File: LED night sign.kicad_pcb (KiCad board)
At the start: 2 copper layers, 42.9 x 36.7 mm, 38 parts, among them Q1 MOSFET-NCH-2N7002PW, Q2 BC817, U1 ATtiny85-20M, U2 APDS-9301

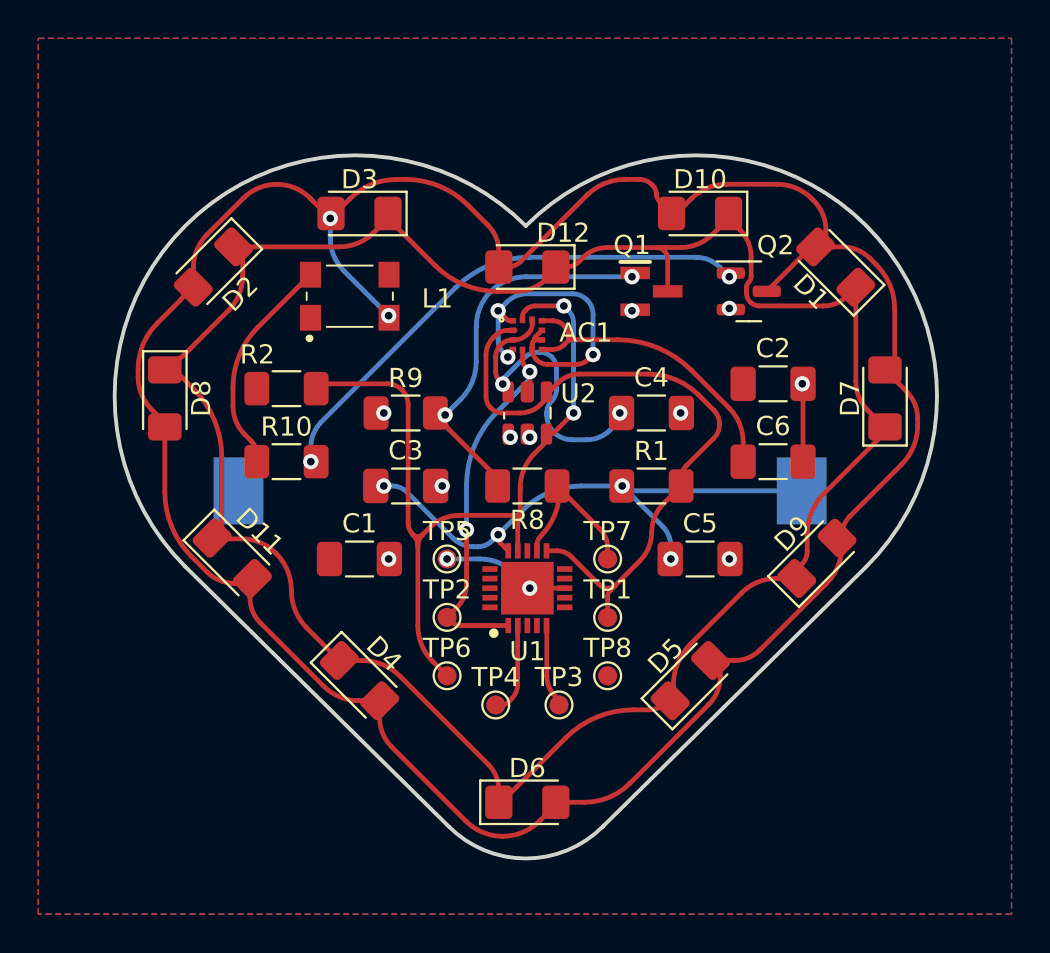
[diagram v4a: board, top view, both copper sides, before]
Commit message: Improved pcb wiring
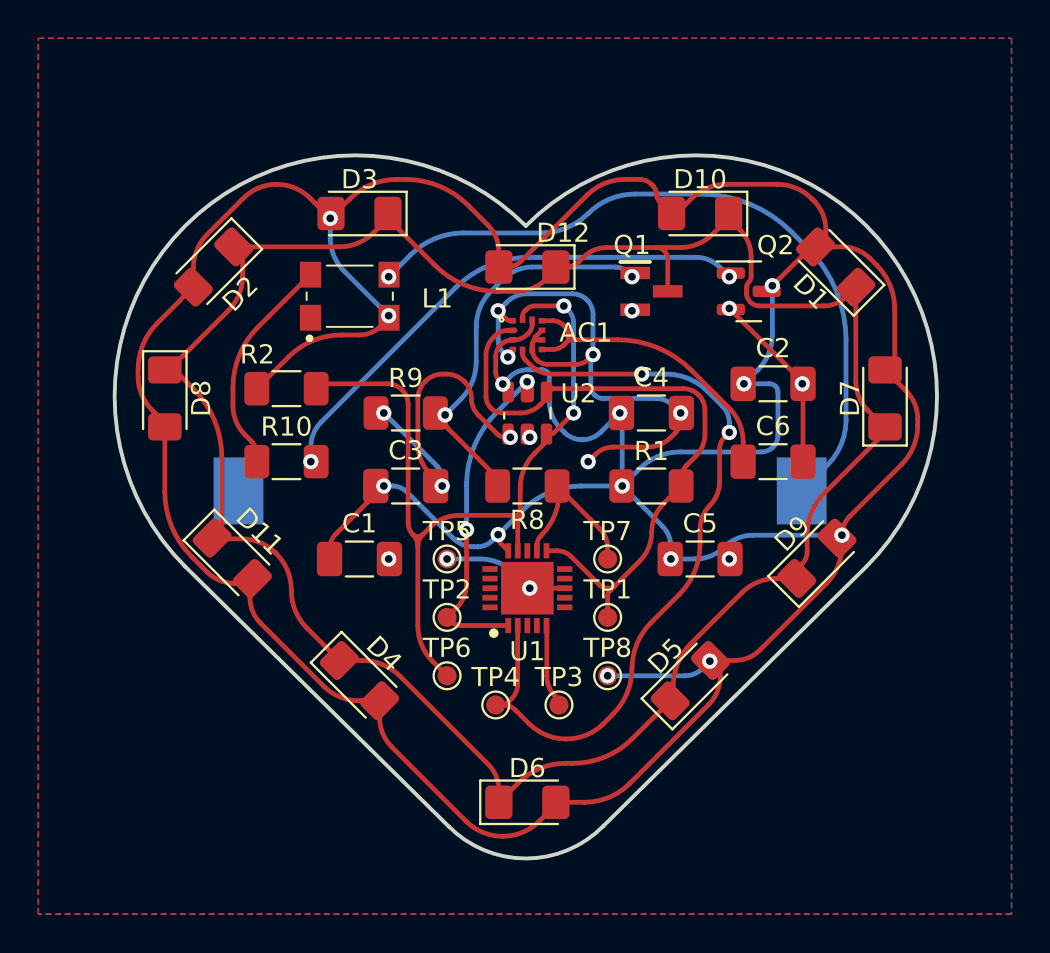
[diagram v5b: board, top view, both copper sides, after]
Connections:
- AC1 pad 11: +3V0 -> JouleThiefPWR
- AC1 pad 3: +3V0 -> JouleThiefPWR
- AC1 pad 5: INT -> INTM
- C1 pad 1: +3V0 -> JouleThiefPWR
- C2 pad 1: +3V0 -> JouleThiefPWR
- C3 pad 1: +3V0 -> JouleThiefPWR
- C4 pad 1: +3V0 -> JouleThiefPWR
- C5 pad 1: +3V0 -> JouleThiefPWR
- R1 pad 1: +3V0 -> JouleThiefPWR
- R2 pad 2: +3V0 -> JouleThiefPWR
- TP2 pad 1: INT -> INTL
- TP4 pad 1: PB3 -> INTM
- TP8 pad 1: +3V0 -> JouleThiefPWR
- U1 pad 1: INT -> INTL
- U1 pad 15: +3V0 -> JouleThiefPWR
- U1 pad 2: PB3 -> INTM
- U2 pad 1: +3V0 -> JouleThiefPWR
- U2 pad 6: INT -> INTL
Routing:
- net JouleThiefPWR: track 139.3 -> 225.3 mm, vias 2 -> 13
- net INTM: track 0.00 -> 41.1 mm, vias 0 -> 2
- net GND: track 28.2 -> 64.1 mm, vias 15 -> 16
- net INT: track 19.8 -> 0.00 mm, vias 2 -> 0
- net INTL: track 0.00 -> 16.9 mm, vias 0 -> 2
- net +3V0: track 47.2 -> 37.8 mm, vias 6 -> 1
- net PB3: track 4.84 -> 0.00 mm
- net PB0/SDA/MOSI: track 35.5 -> 34.6 mm

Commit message: Finished V1.0
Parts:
- added G***: LOGO, LOGO, B.Cu at (149.7, 114.9)
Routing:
- net +3V0: track 37.8 -> 42.6 mm
- added copper zone on F.Cu, net GND
- removed copper zone on F.Cu, net +3V0
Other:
- board text added: "+"
- board text added: "-"
- board text added: "Designed by Casper R. Tak"
- board text added: "My heart beats unexpectedly when I think of you"
